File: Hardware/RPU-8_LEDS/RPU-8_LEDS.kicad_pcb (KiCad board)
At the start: 4 copper layers, 139.7 x 55.9 mm, 17 parts, among them J1 ADDR_BUS, J2 DATA_BUS, J3 Conn_01x03_Female, J4 CTRL_BUS, J5 INST_REG, U1 8_Segment_LED_Bar_Graph, U2 8_Segment_LED_Bar_Graph, U3 8_Segment_LED_Bar_Graph, U4 8_Segment_LED_Bar_Graph, U5 8_Segment_LED_Bar_Graph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

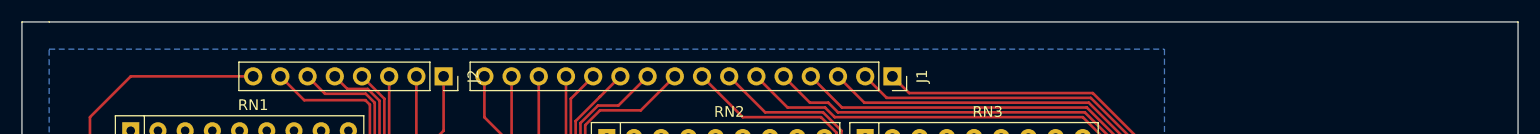
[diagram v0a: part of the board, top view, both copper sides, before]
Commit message: CTRL Board Layout Fixed
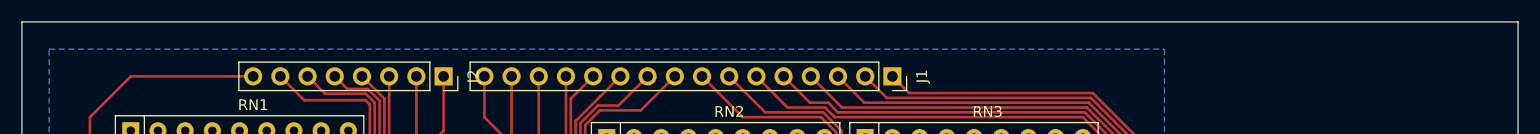
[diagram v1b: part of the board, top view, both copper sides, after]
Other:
- outline, holes or cut-outs redrawn
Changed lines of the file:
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@@
   )
   (gr_line (start 231.14 121.92) (end 91.44 121.92) (layer "Edge.Cuts") (width 0.1))
-  (gr_line (start 93.98 66.04) (end 231.14 66.04) (layer "Edge.Cuts") (width 0.1))
   (gr_line (start 91.44 121.92) (end 91.44 66.04) (layer "Edge.Cuts") (width 0.1))
-  (gr_line (start 91.44 66.04) (end 93.98 66.04) (layer "Edge.Cuts") (width 0.1))
+  (gr_line (start 91.44 66.04) (end 231.14 66.04) (layer "Edge.Cuts") (width 0.1))
   (gr_line (start 231.14 66.04) (end 231.14 121.92) (layer "Edge.Cuts") (width 0.1))
   (gr_text "CADE CPU" (at 133.985 92.71) (layer "F.SilkS")

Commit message: added images
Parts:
- added D1: LED, LED_THT:LED_D1.8mm_W3.3mm_H2.4mm, F.Cu at (209.6, 85.1)
- added J6: Barrel_Jack, Connector_BarrelJack:BarrelJack_Horizontal, F.Cu at (212.1, 73.7)
- added SW1: SW_Push, Button_Switch_THT:SW_PUSH_6mm, F.Cu at (207.0, 91.4)
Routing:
- net CLK: track 0.00 -> 112.6 mm
- net RST: track 0.00 -> 111.8 mm
